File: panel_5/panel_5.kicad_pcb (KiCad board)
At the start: 2 copper layers, 100 x 128.5 mm, 39 parts

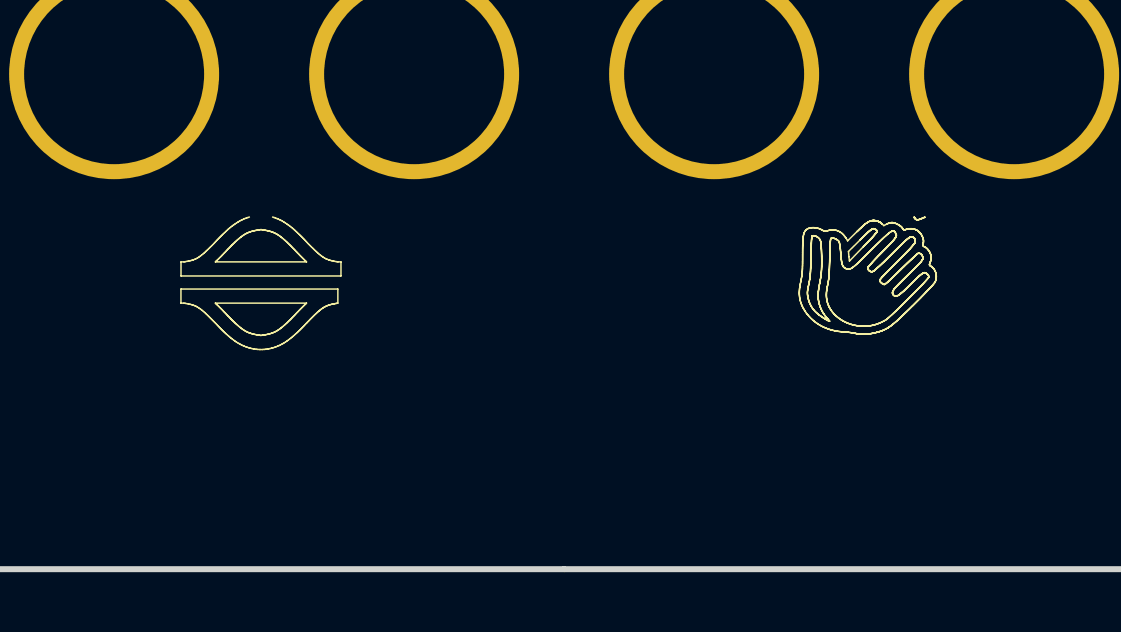
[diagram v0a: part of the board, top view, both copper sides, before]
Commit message: :sparkles: update panels
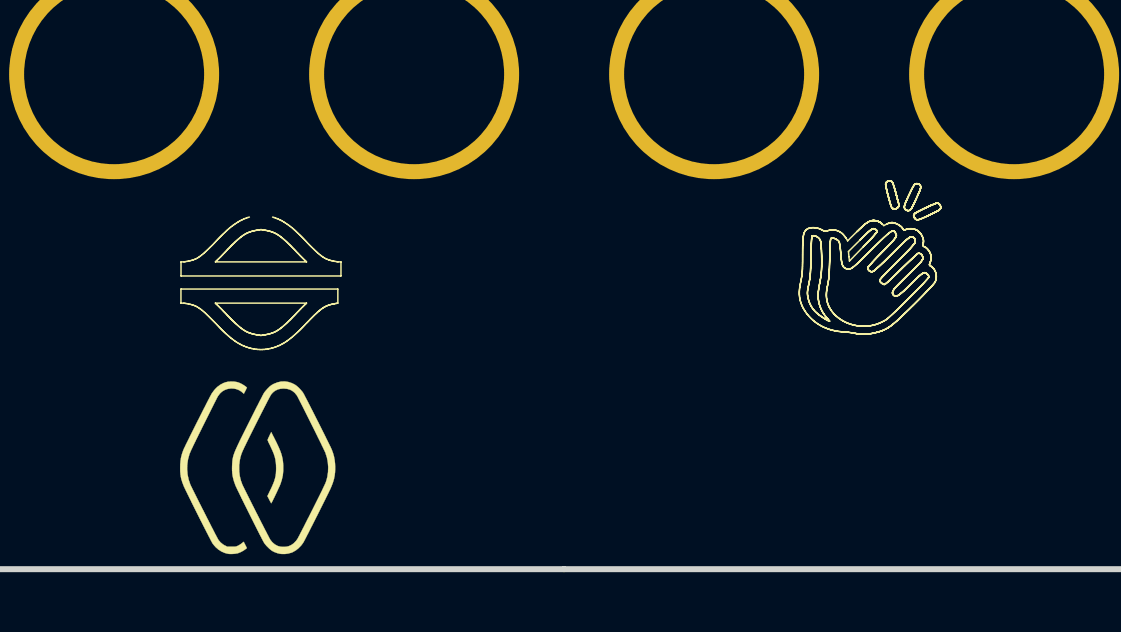
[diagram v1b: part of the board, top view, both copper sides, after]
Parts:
- added G***: LOGO, NN_Footprints:nebularnoise_logo_notext, F.Cu at (99.8, 175.2)
- added G***: LOGO, NN_Footprints:quad5, F.Cu at (100.0, 54.2)
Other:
- board text removed: "Quadrants"
